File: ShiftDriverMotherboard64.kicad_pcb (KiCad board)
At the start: 2 copper layers, 9 parts, among them U1 ShiftDriver, U2 ShiftDriver, U3 ShiftDriver, U4 ShiftDriver, U5 ShiftDriver, U6 ShiftDriver, U7 ShiftDriver, U8 ShiftDriver, U9 TEENSY_3.6_MINIMAL

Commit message: first crack at layout, gonna try laying traces soon
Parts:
- added C1: 10uf, Capacitor_THT:CP_Radial_D5.0mm_P2.00mm, F.Cu at (140.0, 182.5)
- added C2: 0.1uf, Capacitor_THT:C_Disc_D3.0mm_W2.0mm_P2.50mm, F.Cu at (21.2, 148.2)
- added C3: 470uf, Capacitor_THT:CP_Radial_D10.0mm_P5.00mm, F.Cu at (220.8, 181.0)
- added C4: 470uf, Capacitor_THT:CP_Radial_D10.0mm_P5.00mm, F.Cu at (220.8, 168.0)
- added C5: 470uf, Capacitor_THT:CP_Radial_D10.0mm_P5.00mm, F.Cu at (220.8, 155.0)
- added C6: 0.1uf, Capacitor_THT:C_Disc_D3.0mm_W2.0mm_P2.50mm, F.Cu at (202.6, 157.2)
- added C7: 0.1uf, Capacitor_THT:C_Disc_D3.0mm_W2.0mm_P2.50mm, F.Cu at (202.6, 152.8)
- added C8: 10uf, Capacitor_THT:CP_Radial_D5.0mm_P2.00mm, F.Cu at (19.8, 154.5)
- added C9: 10uf, Capacitor_THT:CP_Radial_D5.0mm_P2.00mm, F.Cu at (162.4, 150.5)
- added D1: 1N4001, Diode_THT:D_DO-41_SOD81_P7.62mm_Horizontal, F.Cu at (170.5, 150.5)
- added D2: TEENSY_PWR_IND, LED_THT:LED_D5.0mm, F.Cu at (148.2, 182.0)
- added D3: VDD_IND, LED_THT:LED_D5.0mm, F.Cu at (185.5, 182.0)
- added D4: CLR_LED, LED_THT:LED_D5.0mm, F.Cu at (54.5, 182.0)
- added D5: EN_LED, LED_THT:LED_D5.0mm, F.Cu at (66.5, 182.0)
- added D6: 1N4001, Diode_THT:D_DO-41_SOD81_P7.62mm_Horizontal, F.Cu at (166.8, 150.5)
- added D7: LOCK_IND, LED_THT:LED_D5.0mm, F.Cu at (26.5, 182.0)
- added D8: BOOT_IND, LED_THT:LED_D5.0mm, F.Cu at (78.5, 182.0)
- added D9: VDIG, LED_THT:LED_D5.0mm, F.Cu at (173.5, 182.0)
- added H3: M3/#4-40, HammerheadAudio:M3_MOUNT, F.Cu at (15.0, 185.0)
- added H3: M3/#4-40, HammerheadAudio:M3_MOUNT, F.Cu at (235.0, 100.0)
- added H3: M3/#4-40, HammerheadAudio:M3_MOUNT, F.Cu at (235.0, 185.0)
- added H3: M3/#4-40, HammerheadAudio:M3_MOUNT, F.Cu at (15.0, 100.0)
- added H3: M3/#4-40, HammerheadAudio:M3_MOUNT, F.Cu at (125.0, 15.0)
- added H3: M3/#4-40, HammerheadAudio:M3_MOUNT, F.Cu at (125.0, 185.0)
- added H3: M3/#4-40, HammerheadAudio:M3_MOUNT, F.Cu at (235.0, 15.0)
- added H3: M3/#4-40, HammerheadAudio:M3_MOUNT, F.Cu at (15.0, 15.0)
- added J1: - VSPK_IN +, HammerheadAudio:ScrewTerm+Phoenix_30A_7.62mm_1x2, F.Cu at (199.8, 163.0)
- added J2: PWR OPTION HEADER, Connector_PinHeader_2.54mm:PinHeader_2x04_P2.54mm_Vertical, F.Cu at (173.5, 165.5)
- added J3: V_TNSY_IN, HammerheadAudio:Phoenix_Stacked, F.Cu at (159.0, 182.0)
- added Q1: Q_NPN_EBC, Package_TO_SOT_THT:TO-92L_Inline_Wide, F.Cu at (56.0, 155.0)
- added Q2: Q_NPN_EBC, Package_TO_SOT_THT:TO-92L_Inline_Wide, F.Cu at (60.0, 150.0)
- added R1: 1k, HammerheadAudio:R_THT_P7.62, F.Cu at (66.5, 148.5)
- added R2: 220, HammerheadAudio:R_THT_P7.62, F.Cu at (144.5, 178.5)
- added R3: 220, HammerheadAudio:R_THT_P7.62, F.Cu at (189.2, 178.5)
- added R4: 1k, HammerheadAudio:R_THT_P7.62, F.Cu at (49.5, 148.5)
- added R5: 10k, HammerheadAudio:R_THT_P7.62, F.Cu at (46.5, 148.5)
- added R6: 1k, HammerheadAudio:R_THT_P7.62, F.Cu at (30.3, 178.5)
- added R7: 1k, HammerheadAudio:R_THT_P7.62, F.Cu at (82.2, 178.5)
- added R8: 220, HammerheadAudio:R_THT_P7.62, F.Cu at (169.8, 178.5)
- added SW1: TEENSY_PWR, HammerheadAudio:Tayda_Slide_SPDT, F.Cu at (140.0, 163.5)
- added SW2: BOOT_MODE, HammerheadAudio:Tayda_Slide_SPDT, F.Cu at (110.0, 163.5)
- added SW3: MUTE_SW, HammerheadAudio:Tayda_Slide_SPDT, F.Cu at (125.0, 163.5)
- added U10: LM7805_TO220, Package_TO_SOT_THT:TO-220-3_Horizontal_TabDown, F.Cu at (174.5, 151.5)
- added U11: CD74HC243, Package_DIP:DIP-14_W7.62mm_Socket, F.Cu at (26.8, 156.0)
- added U12: EAPLRAA4, HammerheadAudio:EAPLRAA4, F.Cu at (38.0, 180.2)
- moved U9 11.0 mm to (42.0, 167.5)
- moved U4 6.72 mm to (178.3, 21.0)
- moved U8 6.65 mm to (178.3, 85.0)
- moved U3 4.27 mm to (125.8, 21.0)
- moved U7 4.15 mm to (125.8, 85.0)
- moved U2 1.93 mm to (73.3, 21.0)
- moved U6 1.65 mm to (73.3, 85.0)
- moved U1 1.31 mm to (20.9, 21.0)
- moved U5 0.85 mm to (20.9, 85.0)
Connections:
- U1 pad 1: Net-(U1-Pad1) -> VDD
- U1 pad 2: Net-(U1-Pad2) -> +5V
- U1 pad 3: Net-(U1-Pad3) -> GND
- U1 pad 4: Net-(U1-Pad4) -> D1
- U1 pad 5: Net-(U1-Pad5) -> CS
- U1 pad 6: Net-(U1-Pad6) -> S_CLK
- U1 pad 7: Net-(U1-Pad7) -> CLR
- U1 pad 8: Net-(U1-Pad8) -> EN
- U1 pad 9: Net-(U1-Pad9) -> D2
- U2 pad 1: Net-(U2-Pad1) -> VDD
- U2 pad 2: Net-(U2-Pad2) -> +5V
- U2 pad 3: Net-(U2-Pad3) -> GND
- U2 pad 4: Net-(U2-Pad4) -> D2
- U2 pad 5: Net-(U2-Pad5) -> CS
- U2 pad 6: Net-(U2-Pad6) -> S_CLK
- U2 pad 7: Net-(U2-Pad7) -> CLR
- U2 pad 8: Net-(U2-Pad8) -> EN
- U2 pad 9: Net-(U2-Pad9) -> D3
- U3 pad 1: Net-(U3-Pad1) -> VDD
- U3 pad 2: Net-(U3-Pad2) -> +5V
- U3 pad 3: Net-(U3-Pad3) -> GND
- U3 pad 4: Net-(U3-Pad4) -> D3
- U3 pad 5: Net-(U3-Pad5) -> CS
- U3 pad 6: Net-(U3-Pad6) -> S_CLK
- U3 pad 7: Net-(U3-Pad7) -> CLR
- U3 pad 8: Net-(U3-Pad8) -> EN
- U3 pad 9: Net-(U3-Pad9) -> D4
- U4 pad 1: Net-(U4-Pad1) -> VDD
- U4 pad 2: Net-(U4-Pad2) -> +5V
- U4 pad 3: Net-(U4-Pad3) -> GND
- U4 pad 4: Net-(U4-Pad4) -> D4
- U4 pad 5: Net-(U4-Pad5) -> CS
- U4 pad 6: Net-(U4-Pad6) -> S_CLK
- U4 pad 7: Net-(U4-Pad7) -> CLR
- U4 pad 8: Net-(U4-Pad8) -> EN
- U4 pad 9: Net-(U4-Pad9) -> D5
- U5 pad 1: Net-(U5-Pad1) -> VDD
- U5 pad 2: Net-(U5-Pad2) -> +5V
- U5 pad 3: Net-(U5-Pad3) -> GND
- U5 pad 4: Net-(U5-Pad4) -> D5
- U5 pad 5: Net-(U5-Pad5) -> CS
- U5 pad 6: Net-(U5-Pad6) -> S_CLK
- U5 pad 7: Net-(U5-Pad7) -> CLR
- U5 pad 8: Net-(U5-Pad8) -> EN
- U5 pad 9: Net-(U5-Pad9) -> D6
- U6 pad 1: Net-(U6-Pad1) -> VDD
- U6 pad 2: Net-(U6-Pad2) -> +5V
- U6 pad 3: Net-(U6-Pad3) -> GND
- U6 pad 4: Net-(U6-Pad4) -> D6
- U6 pad 5: Net-(U6-Pad5) -> CS
- U6 pad 6: Net-(U6-Pad6) -> S_CLK
- U6 pad 7: Net-(U6-Pad7) -> CLR
- U6 pad 8: Net-(U6-Pad8) -> EN
- U6 pad 9: Net-(U6-Pad9) -> D7
- U7 pad 1: Net-(U7-Pad1) -> VDD
- U7 pad 2: Net-(U7-Pad2) -> +5V
- U7 pad 3: Net-(U7-Pad3) -> GND
- U7 pad 4: Net-(U7-Pad4) -> D7
- U7 pad 5: Net-(U7-Pad5) -> CS
- U7 pad 6: Net-(U7-Pad6) -> S_CLK
- U7 pad 7: Net-(U7-Pad7) -> CLR
- U7 pad 8: Net-(U7-Pad8) -> EN
- U7 pad 9: Net-(U7-Pad9) -> D8
- U8 pad 1: Net-(U8-Pad1) -> VDD
- U8 pad 2: Net-(U8-Pad2) -> +5V
- U8 pad 3: Net-(U8-Pad3) -> GND
- U8 pad 4: Net-(U8-Pad4) -> D8
- U8 pad 5: Net-(U8-Pad5) -> CS
- U8 pad 6: Net-(U8-Pad6) -> S_CLK
- U8 pad 7: Net-(U8-Pad7) -> CLR
- U8 pad 8: Net-(U8-Pad8) -> EN
- U9 pad 1: Net-(U9-Pad1) -> GND
- U9 pad 11: Net-(U9-Pad11) -> CLR_PIN
- U9 pad 12: Net-(U9-Pad12) -> CS_PIN
- U9 pad 13: Net-(U9-Pad13) -> DAT_PIN
- U9 pad 15: Net-(U9-Pad15) -> +3V3
- U9 pad 34: Net-(U9-Pad34) -> GND
- U9 pad 35: Net-(U9-Pad35) -> CLK_PIN
- U9 pad 36: Net-(U9-Pad36) -> EN_PIN
- U9 pad 37: Net-(U9-Pad37) -> SPDIF
- U9 pad 46: Net-(U9-Pad46) -> +3V3
- U9 pad 48: Net-(U9-Pad48) -> +5V
- U9 pad 7: Net-(U9-Pad7) -> BOOT_IND2
- U9 pad 8: Net-(U9-Pad8) -> BOOT_IND1
- U9 pad 9: Net-(U9-Pad9) -> LOCK_PIN
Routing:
- added copper zone on B.Cu, net GND
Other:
- board outline added: 230 x 180 mm
- board text added: "+"
- board text added: "-"
- board text added: "- VAUX_IN +"
- board text added: "AUDIO BOOT MODE: GREEN = EXTERNAL YELLOW = BUILTIN"
- board text added: "BLTN<-BOOT->EXT"
- board text added: "BOOT MODE"
- board text added: "CLR"
- board text added: "EN / MUTE"
- board text added: "LOCK / READ"
- board text added: "MUTE OUTPUTS"
- board text added: "MUTE<——>UNMUTE"
- board text added: "OFF<-VDIG->ON"
- board text added: "PWR VDIG"
- board text added: "PWR_OPTION"
- board text added: "SPDIF_IN"
- board text added: "VAUX_IND"
- board text added: "VAUX_TO_REG"
- board text added: "VAUX_TO_VDIG"
- board text added: "VDIG_IND"
- board text added: "VSPK_IND"
- board text added: "VSPK_TO_REG"
- board text added: "VSPK_TO_VDIG"

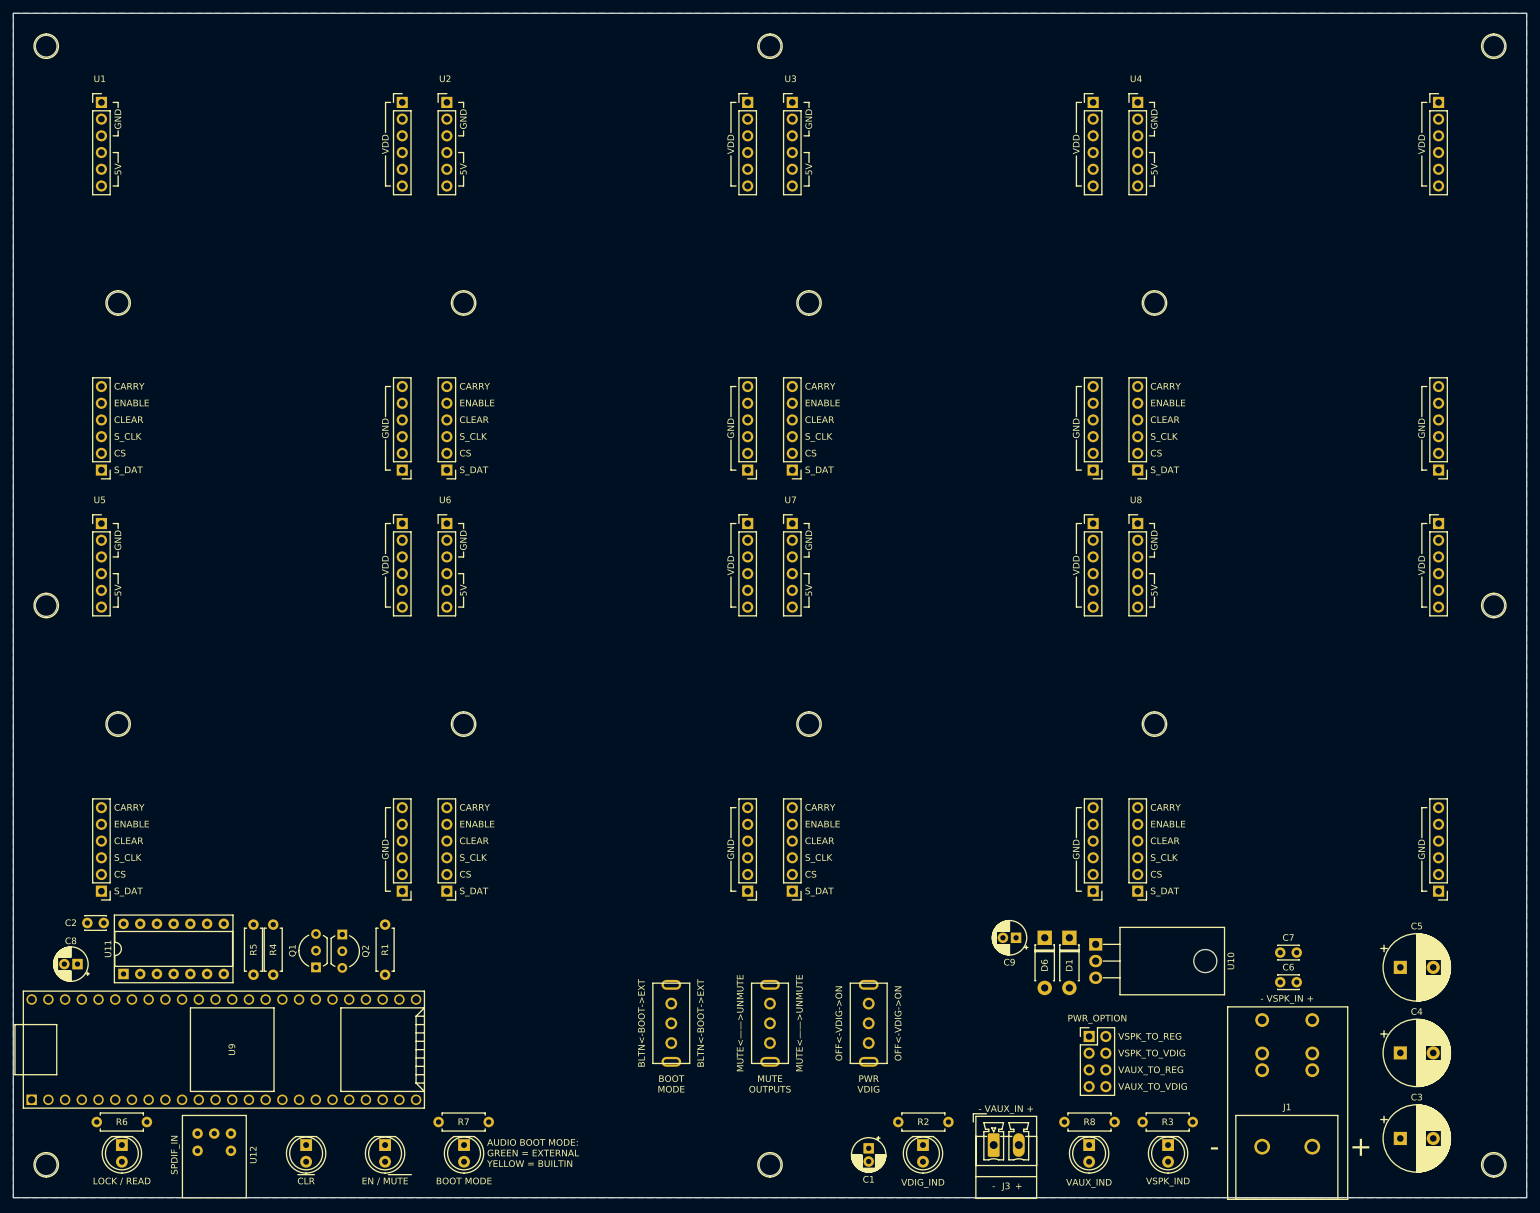
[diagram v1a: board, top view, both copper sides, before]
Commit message: start on power planes
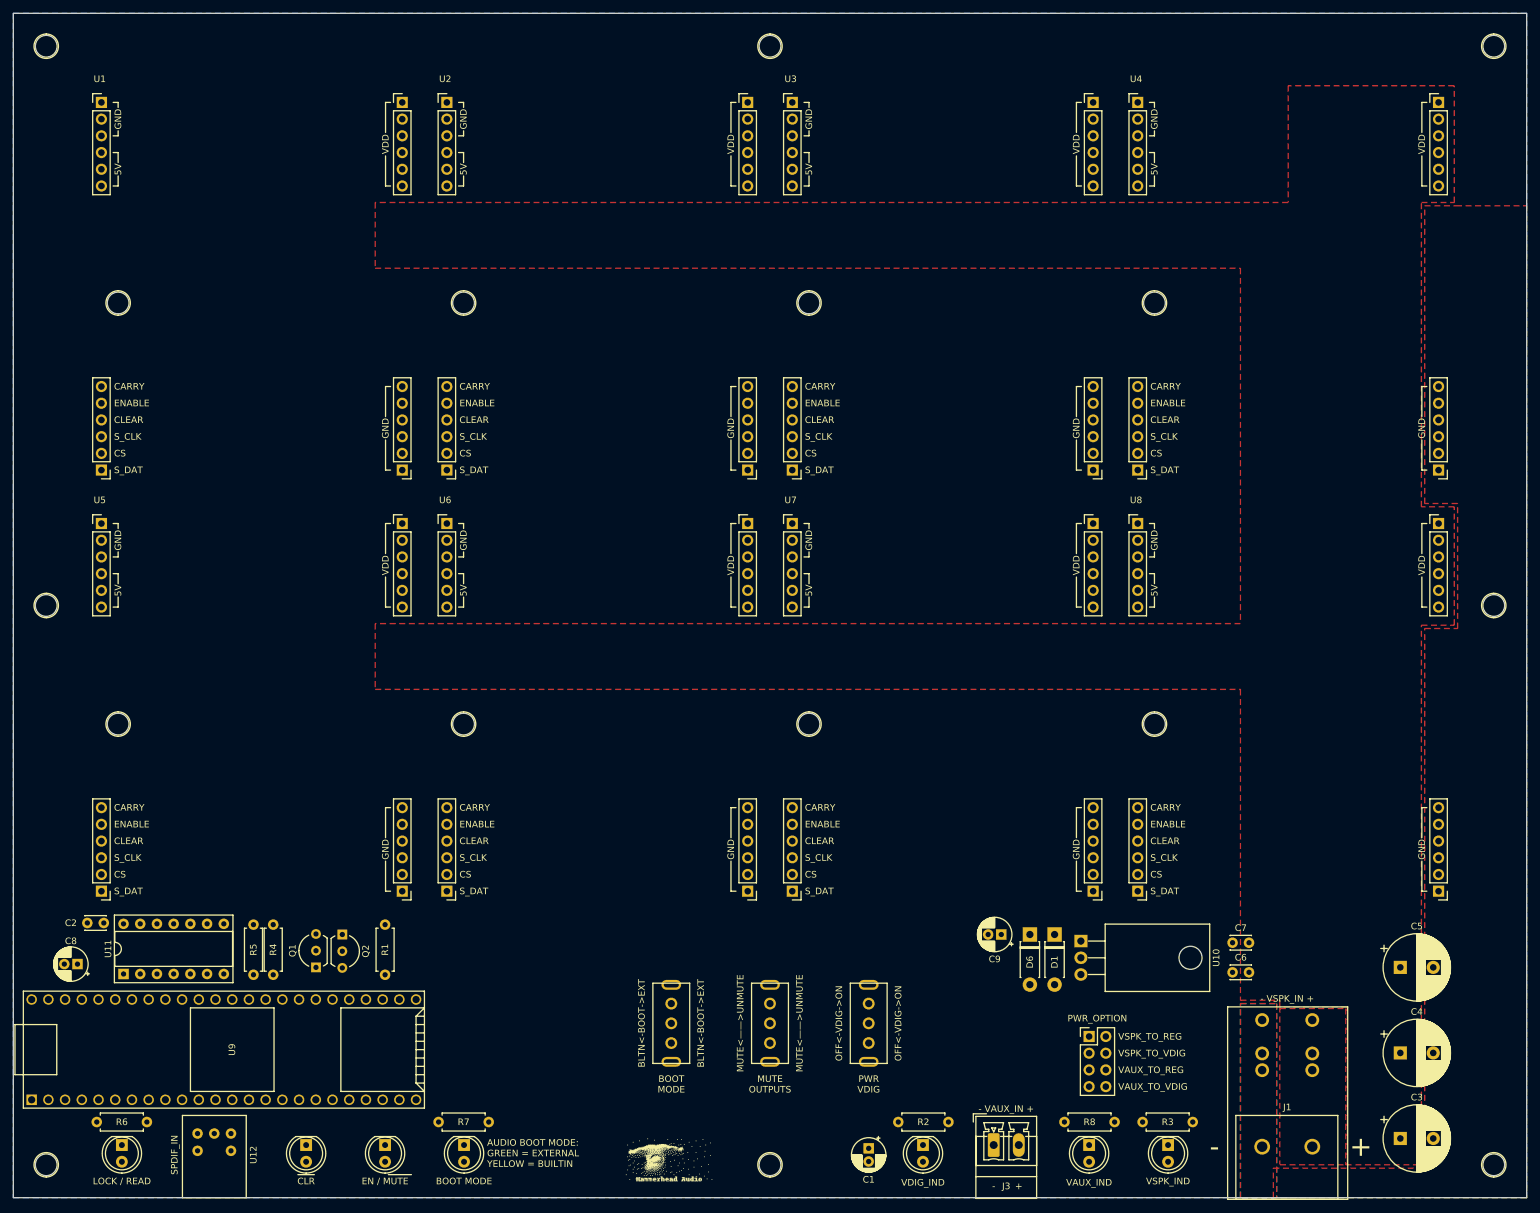
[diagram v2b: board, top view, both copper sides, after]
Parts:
- added HH_LOGO_13.5x6.75: , HammerheadAudio:HH_LOGO_13.5x6.75, F.Cu at (103.0, 181.0)
- moved C6 7.40 mm to (195.3, 155.8)
- moved C7 7.40 mm to (195.3, 151.2)
- moved C9 2.30 mm to (160.2, 150.0)
- moved D1 2.30 mm to (168.2, 150.0)
- moved D6 2.30 mm to (164.5, 150.0)
- moved U10 2.30 mm to (172.2, 151.0)
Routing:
- added copper zone on F.Cu, net GND
- added copper zone on F.Cu, net VDD
